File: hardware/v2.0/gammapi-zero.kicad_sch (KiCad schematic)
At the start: 30 parts, among them J1 Conn_02x20_Counter_Clockwise, SW1 SW_Push, SW2 SW_Push, U1 ECP5U-25F-CABGA256, Y1 SG-8018CG 50.000000MHz

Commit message: Minor changes
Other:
- note added: "GammaPi Zero v2.7!"
- note removed: "GammaPi Zero v2.6!"
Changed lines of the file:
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@@
 		(comment 9 "OSHWA FR000026")
 	)
-	(text "GammaPi Zero v2.6!"
+	(text "GammaPi Zero v2.7!"
 		(exclude_from_sim no)
 		(at 135.89 18.542 0)

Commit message: JLCPCB profile
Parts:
- LED1, LED2, LED3, LED4, LED5: LCSC Part # (none) -> C7429437
- U1: LCSC Part # (none) -> C1521614
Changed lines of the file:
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@@
 	(title_block
 		(title "GammaPi Zero")
-		(date "2026-02-08")
-		(rev "v2.7.0")
+		(date "2026-02-28")
+		(rev "v2.7.1")
 		(company "Vadym Vikulin, Chengyin Yao (cheyao)")
 		(comment 1 "https://github.com/vikulin/gammapi-zero")
@@
 			)
 		)
+		(property "LCSC Part #" "C7429437"
+			(at 54.61 147.32 0)
+			(effects
+				(font
+					(size 1.27 1.27)
+				)
+				(hide yes)
+			)
+		)
 		(pin "3"
 		)
@@
 			)
 		)
+		(property "LCSC Part #" "C1521614"
+			(at 179.07 120.65 0)
+			(effects
+				(font
+					(size 1.27 1.27)
+				)
+				(hide yes)
+			)
+		)
 		(pin "P10"
 		)
@@
 			)
 		)
+		(property "LCSC Part #" "C7429437"
+			(at 54.61 114.3 0)
+			(effects
+				(font
+					(size 1.27 1.27)
+				)
+				(hide yes)
+			)
+		)
 		(pin "3"
 		)
@@
 			)
 		)
+		(property "LCSC Part #" "C1521614"
+			(at 104.14 121.92 0)
+			(effects
+				(font
+					(size 1.27 1.27)
+				)
+				(hide yes)
+			)
+		)
 		(pin "T2"
 		)
@@
 			)
 		)
+		(property "LCSC Part #" "C7429437"
+			(at 54.61 163.83 0)
+			(effects
+				(font
+					(size 1.27 1.27)
+				)
+				(hide yes)
+			)
+		)
 		(pin "3"
 		)
@@
 			)
 		)
+		(property "LCSC Part #" "C7429437"
+			(at 54.61 130.81 0)
+			(effects
+				(font
+					(size 1.27 1.27)
+				)
+				(hide yes)
+			)
+		)
 		(pin "3"
 		)
@@
 			(at 54.61 180.34 0)
 			(effects
+				(font
+					(size 1.27 1.27)
+				)
+				(hide yes)
+			)
+		)
+		(property "LCSC Part #" "C7429437"
+			(at 54.61 180.34 0)
+			(effects

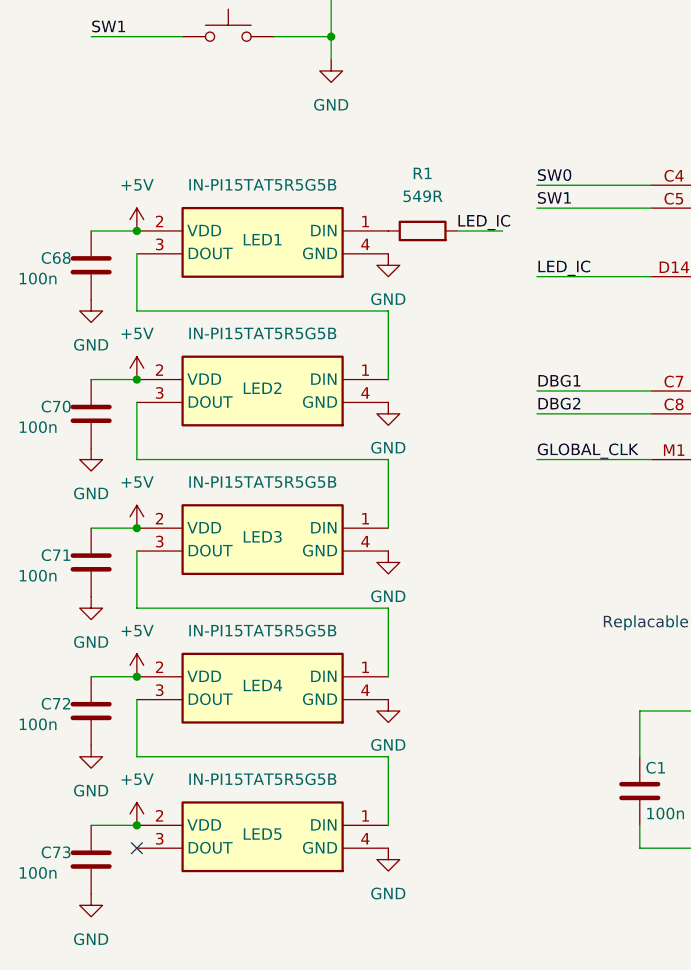
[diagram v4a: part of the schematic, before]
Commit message: WS2812B-2020 LED Update
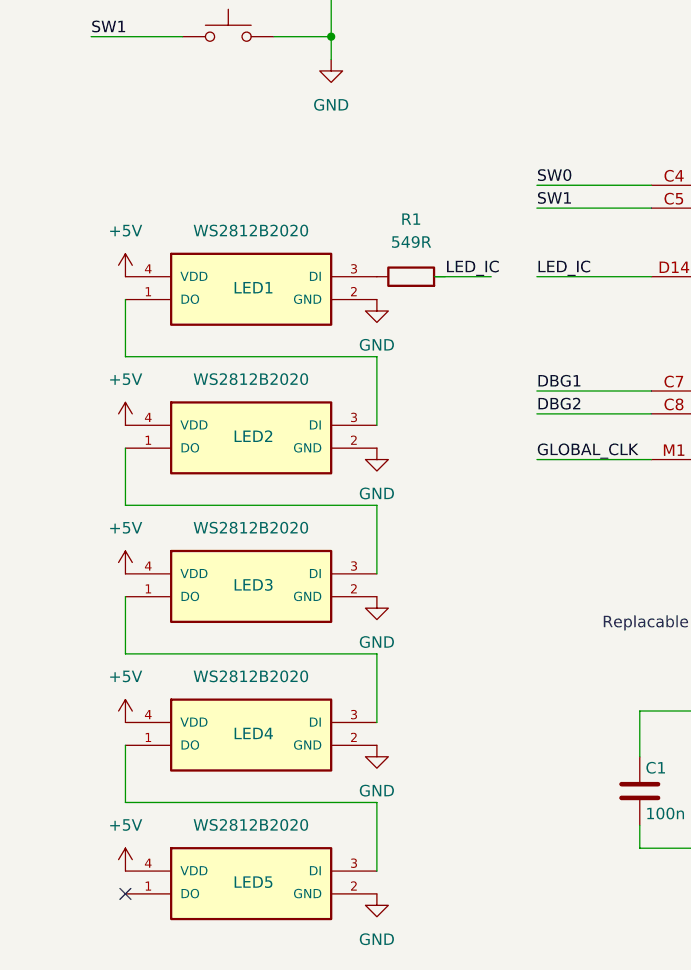
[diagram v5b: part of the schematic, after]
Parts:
- removed C68, C70, C71, C72, C73: 100n, Capacitor_SMD:C_0402_1005Metric, symbol Device:C
- removed LED1, LED2, LED3, LED4, LED5: IN-PI15TAT5R5G5B, INPI15TAT5R5G5B, symbol IN-PI15TAT5R5G5B:IN-PI15TAT5R5G5B
- added LED1, LED2, LED3, LED4, LED5: WS2812B2020, WS2812B2020:LED_WS2812B2020, symbol WS2812B2020:WS2812B2020
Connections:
- net +5V: now also LED1.4 (VDD), LED2.4 (VDD), LED3.4 (VDD), LED4.4 (VDD), LED5.4 (VDD)
- net GND: now also LED1.2 (GND), LED2.2 (GND), LED3.2 (GND), LED4.2 (GND), LED5.2 (GND)
- net at R1.1: now also LED1.3 (DI)
- new net: LED4.1 (DO), LED5.3 (DI)
- new net: LED3.1 (DO), LED4.3 (DI)
- new net: LED2.1 (DO), LED3.3 (DI)
- new net: LED1.1 (DO), LED2.3 (DI)
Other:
- moved on the sheet: R1

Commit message: Capacitor update
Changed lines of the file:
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@@
 	(wire
 		(pts
-			(xy 59.69 116.84) (xy 66.04 116.84)
+			(xy 60.96 116.84) (xy 67.31 116.84)
 		)
 		(stroke
@@
 	)
 	(label "LED_IC"
-		(at 60.96 116.84 0)
-		(effects
-			(font
-				(size 1.27 1.27)
-			)
-			(justify left bottom)
-		)
-	)
+		(at 67.31 116.84 180)
+		(effects
+			(font
+				(size 1.27 1.27)
+			)
+			(justify right bottom)
+		)
+	)
